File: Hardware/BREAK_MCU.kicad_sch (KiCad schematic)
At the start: 51 parts, among them Q13 NCE01ND03S, Q14 NCE01ND03S, U24 PY32F002BF15U, U25 EG2104, U26 ZX-HY2.0-2PWT, U27 RT9193-33GB-MS, U28 EG2104, U29 ZX-HY2.0-2PWT, U30 RS622XTDE8

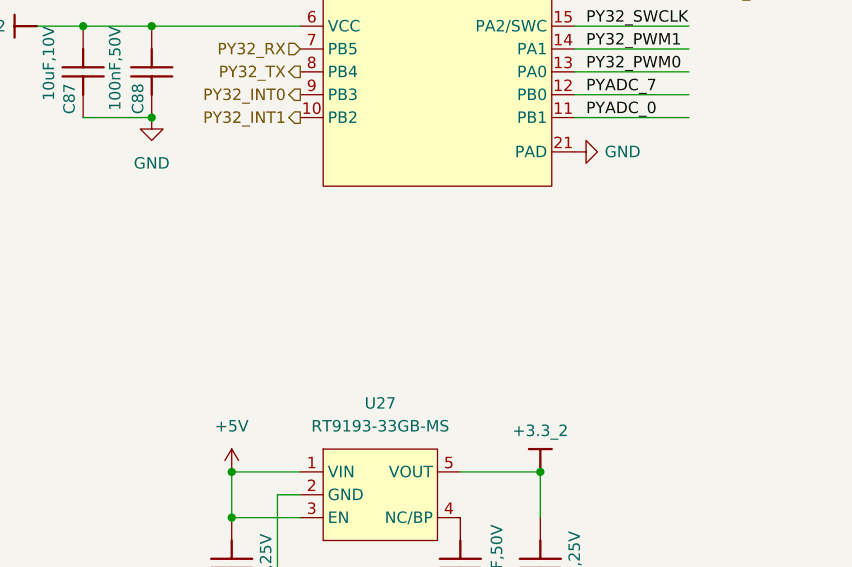
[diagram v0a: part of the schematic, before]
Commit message: 新增ESC IO引出，ESC CTR LED，EUI接口
编码器接口电源输出加保险，SPI加ESD
PY32ADC外部接口加ESD
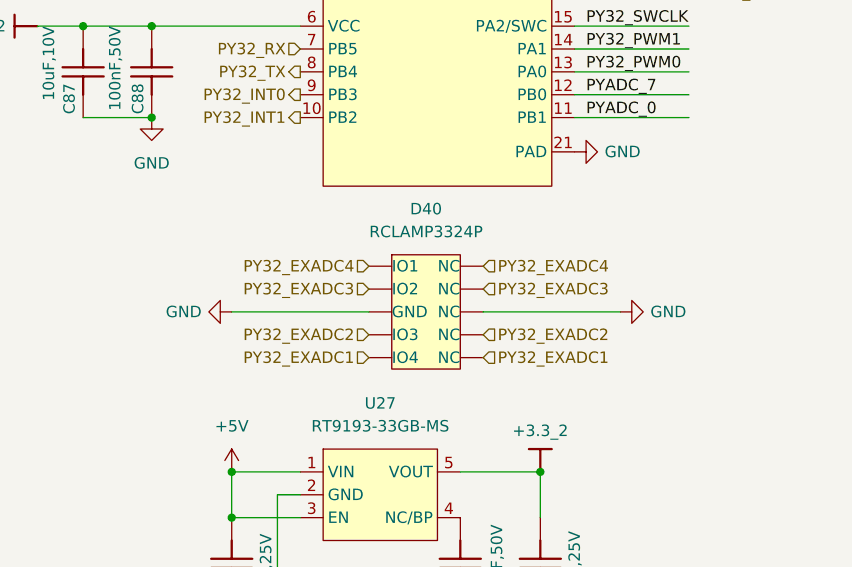
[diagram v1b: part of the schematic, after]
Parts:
- added D40: RCLAMP3324P, Package_DFN_QFN:Diodes_UDFN-10_1.0x2.5mm_P0.5mm, symbol HPM6280Foc:RCLAMP3324P
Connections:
- net GND: now also D40.3 (GND), D40.8 (NC)
- net PY32_EXADC1: now also D40.5 (IO4), D40.6 (NC)
- net PY32_EXADC2: now also D40.4 (IO3), D40.7 (NC)
- net PY32_EXADC3: now also D40.2 (IO2), D40.9 (NC)
- net PY32_EXADC4: now also D40.1 (IO1), D40.10 (NC)

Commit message: 拉线
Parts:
- added U53: 74LVC1G08, Package_TO_SOT_SMD:SOT-353_SC-70-5, symbol 74xGxx:74LVC1G08
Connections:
- net VBUS: now also Q13.5 (D1), Q13.6 (D1), Q14.5 (D1), Q14.6 (D1); no longer Q13.7 (D2), Q13.8 (D2), Q14.7 (D2), Q14.8 (D2)
- net at R66.1, R68.1, R70.1: now also U30.3 (+INB); no longer U30.5 (+INB)
- net at C91.2, Q14.5 (D1), Q14.6 (D1)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: now also Q14.3 (S1); no longer Q14.1 (S2)
- net at C85.2, Q13.5 (D1), Q13.6 (D1)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: now also Q13.3 (S1); no longer Q13.1 (S2)
- net at D28.2 (A), R62.2: now also Q14.4 (G1); no longer Q14.2 (G2)
- net at D25.2 (A), R59.2: now also Q13.4 (G1); no longer Q13.2 (G2)
- net at R72.2, R75.2: now also U30.1 (OUTB); no longer U30.7 (OUTB)
- net at R74.1, R75.1: now also U30.2 (-INB); no longer U30.6 (-INB)
- net PY32_RST renamed ~{PY32_RST}

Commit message: 修存档拉线
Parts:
- removed Q13, Q14: NCE01ND03S, Package_SO:SOP-8_3.9x4.9mm_P1.27mm, symbol HPM6280Foc:NCE01ND03S
- removed U30: RS622XTDE8, Package_DFN_QFN:DFN-8-1EP_2x2mm_P0.5mm_EP0.6x1.2mm, symbol HPM6280Foc:RS622XTDE8
- removed U53: 74LVC1G08, Package_TO_SOT_SMD:SOT-353_SC-70-5, symbol 74xGxx:74LVC1G08
- added J24: WAFER-GH1.25-4PLB, Connector_JST:JST_SH_BM04B-SRSS-TB_1x04-1MP_P1.00mm_Vertical, symbol HPM6280Foc:WAFER-SH1.0-4PLB
- renumbered C84 to C65, C85 to C66, C86 to C67, C87 to C68, C88 to C69, C90 to C70, C91 to C71, C92 to C72, C93 to C73, C94 to C74, C95 to C75, C97 to C76, C98 to C77, C99 to C78, D24 to D32, D25 to D33, D26 to D34, D40 to D35, D27 to D36, D28 to D37, D29 to D38, NT13 to NT17, NT14 to NT18, NT15 to NT19, NT16 to NT20, Q13 to Q14, Q14 to Q16, R59 to R61, R60 to R62, R61 to R63, R62 to R64, R63 to R65, R64 to R66, R65 to R67, R66 to R68, R67 to R69, R68 to R70, R69 to R71, R70 to R72, R71 to R73, R72 to R74, R73 to R75, R74 to R76, R75 to R77, R76 to R78, U24 to U28, U25 to U29, U26 to U30, U27 to U31, U28 to U32, U29 to U33, U30 to U35
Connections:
- net +3.3_2: now also J24.1 (Pin_1)
- net GND: now also J24.4 (Pin_4), J24.MP (MountPin)
- net PY32_SWCLK: now also J24.3 (Pin_3)
- net PY32_SWDIO: now also J24.2 (Pin_2)
- net VBUS: now also Q14.7 (D2), Q14.8 (D2), Q16.7 (D2), Q16.8 (D2)
- net at R68.1, R70.1, R72.1: now also U35.5 (+INB)
- net at C71.2, Q16.5 (D1), Q16.6 (D1)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: now also Q16.1 (S2)
- net at C66.2, Q14.5 (D1), Q14.6 (D1)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: now also Q14.1 (S2)
- net at D37.2 (A), R64.2: now also Q16.2 (G2)
- net at D33.2 (A), R61.2: now also Q14.2 (G2)
- net at R74.2, R77.2: now also U35.7 (OUTB)
- net at R76.1, R77.1: now also U35.6 (-INB)
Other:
- moved on the sheet: C73, C74, C75, U31

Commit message: 拉线
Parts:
- added C142, C143: 100nF,50V, Capacitor_SMD:C_0402_1005Metric, symbol HPM6280Foc:CC0402KRX7R7BB104
- added unit 2 of Q14
- added unit 2 of Q16
- added unit 1 of U35
- added U36, U37: 74LVC1G08, Package_TO_SOT_SMD:SOT-353_SC-70-5, symbol 74xGxx:74LVC1G08
- C69: footprint Capacitor_SMD:C_0603_1608Metric -> Capacitor_SMD:C_0402_1005Metric; symbol HPM6280Foc:CC0603KRX7R9BB104 -> HPM6280Foc:CC0402KRX7R7BB104; 华秋编号 G0045361 -> G0042289; 立创编号 C14663 -> C60474
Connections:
- net +3.3_2: now also C142.1, C143.1, U35.8 (V+), U36.5 (VCC), U37.5 (VCC); no longer U35.8 (V+)
- net GND: now also C142.2, C143.2, U35.4 (V-), U35.9 (PAD), U36.3 (GND), U37.3 (GND); no longer U35.4 (V-), U35.9 (PAD)
- net PY32_BRK: now also U36.2, U37.2
- net PY32_SD0: now also U28.2 (PC1), U36.1; no longer U28.3 (PB7), U29.3 (SD)
- net PY32_SD1: now also U28.3 (PB7), U37.1; no longer U28.2 (PC1), U32.3 (SD)
- net VBUS: now also Q14.7 (D2), Q14.8 (D2), Q16.7 (D2), Q16.8 (D2); no longer Q14.7 (D2), Q14.8 (D2), Q16.7 (D2), Q16.8 (D2)
- net at C71.2, Q16.5 (D1), Q16.6 (D1)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: now also Q16.1 (S2); no longer Q16.1 (S2)
- net at R73.2, R78.2: now also U35.1 (OUTB); no longer U35.1 (OUTB)
- net at R75.1, R78.1: now also U35.2 (-INB); no longer U35.2 (-INB)
- net at R67.1, R69.1, R71.1: now also U35.3 (+INB); no longer U35.3 (+INB)
- net at D37.2 (A), R64.2: now also Q16.2 (G2); no longer Q16.2 (G2)
- net at C66.2, Q14.5 (D1), Q14.6 (D1)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: now also Q14.1 (S2); no longer Q14.1 (S2)
- net at D33.2 (A), R61.2: now also Q14.2 (G2); no longer Q14.2 (G2)
- new net SD0: U29.3 (SD), U36.4
- new net SD1: U32.3 (SD), U37.4
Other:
- note added: "硬件STO"
- moved on the sheet: C78
